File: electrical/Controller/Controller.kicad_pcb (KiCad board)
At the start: 2 copper layers, 72 x 20 mm, 30 parts, among them J1 USB4145-03-0170-C, J3 TC2030-NL, U1 LP5912-3.3DRV, U2 USBLC6-2P6, U3 STM32L072CBTx

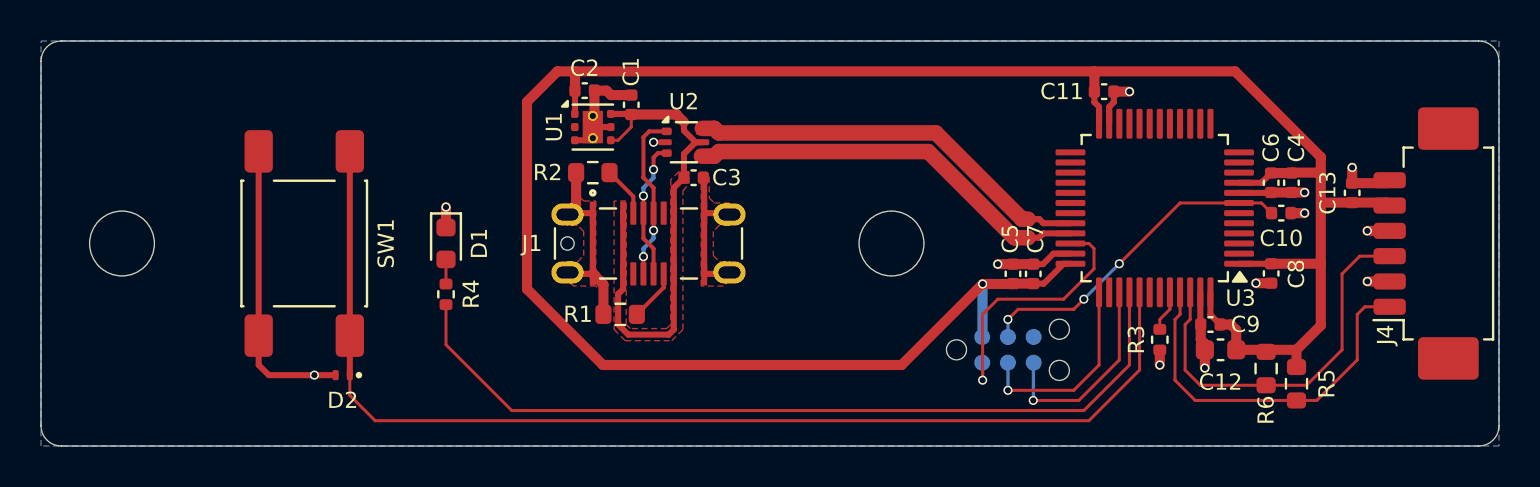
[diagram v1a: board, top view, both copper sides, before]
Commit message: Remove UART from debug connector
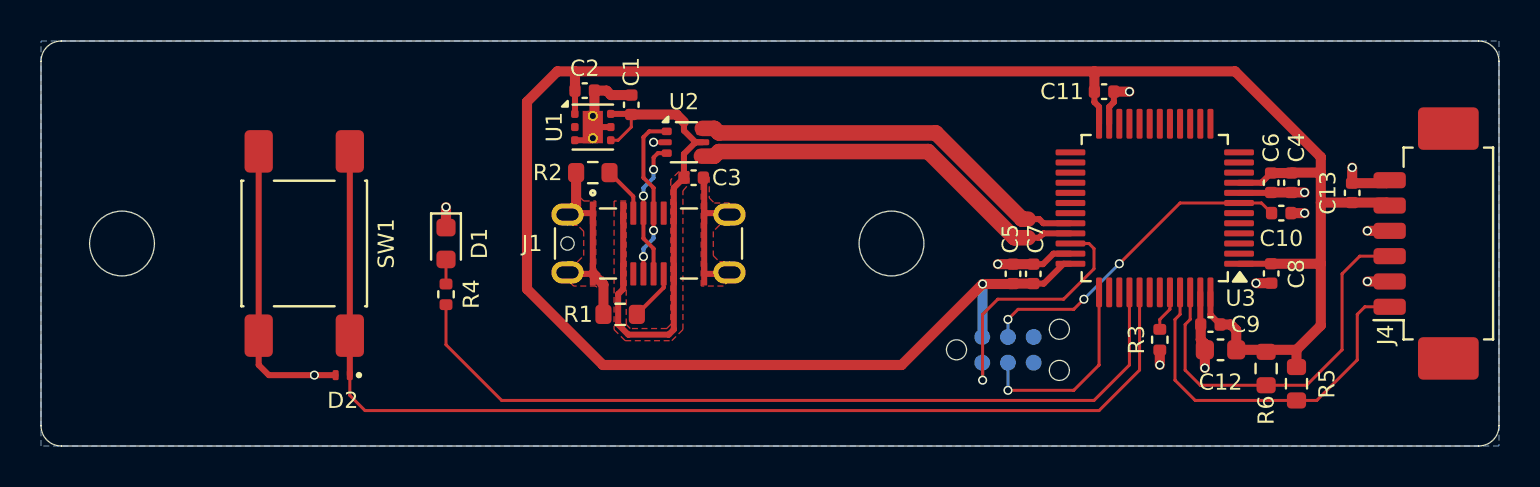
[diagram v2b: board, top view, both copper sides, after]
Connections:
- J3 pad 6: UART_TX -> unconnected-(J3-SWO-Pad6)
- U3 pad 39: UART_TX -> unconnected-(U3-PB3-Pad39)
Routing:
- net UART_TX: track 10.3 -> 0.00 mm, vias 1 -> 0
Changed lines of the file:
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@@
 	(net 10 "unconnected-(U3-PB14-Pad27)")
 	(net 11 "unconnected-(U3-PB13-Pad26)")
-	(net 12 "UART_TX")
+	(net 12 "unconnected-(J3-SWO-Pad6)")
 	(net 13 "/SWDIO")
 	(net 14 "/I2C_SCL")
@@
 	(net 51 "Net-(U3-PB4)")
 	(net 52 "Net-(D2-K)")
+	(net 53 "unconnected-(U3-PB3-Pad39)")
 	(footprint "MountingHole:MountingHole_3.2mm_M3"
 		(layer "F.Cu")
@@
 			(layers "F.Cu" "F.Mask" "F.Paste")
 			(roundrect_rratio 0.25)
-			(net 12 "UART_TX")
+			(net 53 "unconnected-(U3-PB3-Pad39)")
 			(pinfunction "PB3")
-			(pintype "bidirectional")
+			(pintype "bidirectional+no_connect")
 		)
 		(pad "40" smd roundrect
@@
 			(size 0.7874 0.7874)
 			(layers "B.Cu" "B.Mask")
-			(net 12 "UART_TX")
+			(net 12 "unconnected-(J3-SWO-Pad6)")
 			(pinfunction "SWO")
-			(pintype "input")
+			(pintype "input+no_connect")
 		)
 		(zone
@@
 	)
 	(segment
-		(start 167.25 86.75)
-		(end 169.25 84.75)
-		(width 0.15)
-		(layer "F.Cu")
-		(net 12)
-	)
-	(segment
-		(start 165 86.75)
-		(end 167.25 86.75)
-		(width 0.15)
-		(layer "F.Cu")
-		(net 12)
-	)
-	(segment
-		(start 169.25 84.75)
-		(end 169.25 81.4125)
-		(width 0.15)
-		(layer "F.Cu")
-		(net 12)
-	)
-	(via
-		(at 165 86.75)
-		(size 0.45)
-		(drill 0.3)
-		(layers "F.Cu" "B.Cu")
-		(net 12)
-	)
-	(segment
-		(start 165 84.905)
-		(end 165.02 84.885)
-		(width 0.15)
-		(layer "B.Cu")
-		(net 12)
-	)
-	(segment
-		(start 165 86.75)
-		(end 165 84.905)
-		(width 0.15)
-		(layer "B.Cu")
-		(net 12)
-	)
-	(segment
 		(start 168 80.25)
 		(end 168 79.25)
@@
 	)
 	(segment
-		(start 139.25 87.25)
-		(end 167.5 87.25)
+		(start 136 84)
+		(end 138.75 86.75)
 		(width 0.15)
 		(layer "F.Cu")
@@
 	)
 	(segment
-		(start 136 84)
-		(end 139.25 87.25)
+		(start 136 82.02)
+		(end 136 84)
 		(width 0.15)
 		(layer "F.Cu")
@@
 	)
 	(segment
-		(start 167.5 87.25)
+		(start 168 86.75)
 		(end 169.75 85)
 		(width 0.15)
@@
 	)
 	(segment
-		(start 169.75 85)
-		(end 169.75 81.4125)
+		(start 138.75 86.75)
+		(end 168 86.75)
 		(width 0.15)
 		(layer "F.Cu")
@@
 	)
 	(segment
-		(start 136 82.02)
-		(end 136 84)
+		(start 169.75 85)
+		(end 169.75 81.4125)
 		(width 0.15)
 		(layer "F.Cu")
@@
 	)
 	(segment
-		(start 131.25 86.5)
-		(end 131.25 85.5)
+		(start 170.25 81.4125)
+		(end 170.25 85.25)
 		(width 0.15)
 		(layer "F.Cu")
@@
 	)
 	(segment
-		(start 131.25 74.45)
-		(end 131.25 83.55)
-		(width 0.3)
+		(start 168.25 87.25)
+		(end 132 87.25)
+		(width 0.15)
 		(layer "F.Cu")
 		(net 52)
 	)
 	(segment
-		(start 170.25 81.4125)
-		(end 170.25 85.25)
+		(start 131.25 86.5)
+		(end 131.25 85.5)
 		(width 0.15)
 		(layer "F.Cu")
@@
 	)
 	(segment
-		(start 132.5 87.75)
-		(end 131.25 86.5)
+		(start 170.25 85.25)
+		(end 168.25 87.25)
 		(width 0.15)
 		(layer "F.Cu")
@@
 	)
 	(segment
-		(start 170.25 85.25)
-		(end 167.75 87.75)
-		(width 0.15)
+		(start 131.25 74.45)
+		(end 131.25 83.55)
+		(width 0.3)
 		(layer "F.Cu")
 		(net 52)
 	)
 	(segment
-		(start 167.75 87.75)
-		(end 132.5 87.75)
+		(start 132 87.25)
+		(end 131.25 86.5)
 		(width 0.15)
 		(layer "F.Cu")

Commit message: Use REVISION var to fill silkscreen
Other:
- board text added: "MIDI Concertina Controller - Rev ${REVISION}"
- board text removed: "MIDI Concertina Controller - Rev 1"
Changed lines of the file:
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@@
 		(layer "User.2")
 	)
-	(gr_text "MIDI Concertina Controller - Rev 1"
+	(gr_text "MIDI Concertina Controller - Rev ${REVISION}"
 		(at 187 70.25 0)
 		(layer "B.SilkS")

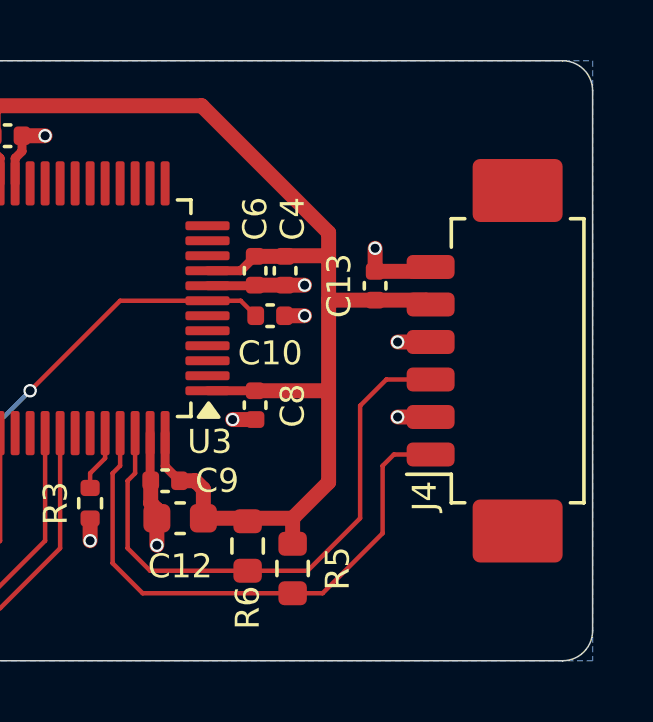
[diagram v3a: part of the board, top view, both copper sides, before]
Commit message: Replace PicoBlade connectors with SKEDD
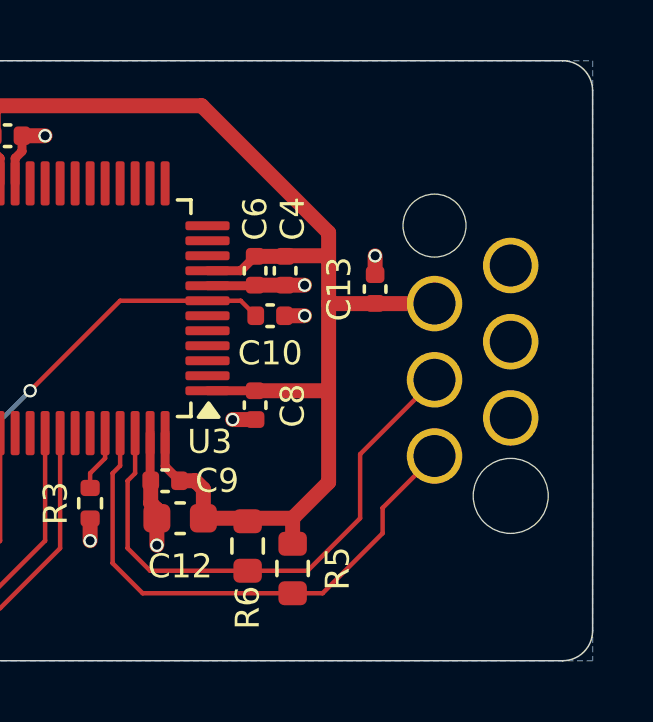
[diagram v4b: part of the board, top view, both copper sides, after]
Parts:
- J4: value ~ -> I2C; footprint Connector_Molex:Molex_PicoBlade_53261-0671_1x06-1MP_P1.25mm_Horizontal -> MidiConcertina:Wuerth_WR-WST_490107670612_2x03_P2.54mm_SKEDD; moved to B.Cu
- moved J4 1.00 mm to (184.0, 79.0), turned to 0 degrees
- moved C13 0.11 mm to (180.8, 76.6)
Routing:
- net GND: track 58.6 -> 54.4 mm, vias 13 -> 11
- net /I2C_SDA: track 19.2 -> 18.4 mm
- net /I2C_SCL: track 18.7 -> 18.0 mm
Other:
- board text added: "MIDI Concertina Controller Rev ${REVISION}"
- board text removed: "MIDI Concertina Controller - Rev ${REVISION}"

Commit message: Relabel components
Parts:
- renumbered J3 to J2, J4 to J3
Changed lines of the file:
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@@
 	(net 10 "unconnected-(U3-PB14-Pad27)")
 	(net 11 "unconnected-(U3-PB13-Pad26)")
-	(net 12 "unconnected-(J3-SWO-Pad6)")
+	(net 12 "unconnected-(J2-SWO-Pad6)")
 	(net 13 "/SWDIO")
 	(net 14 "/I2C_SCL")
@@
 		(layer "B.Cu")
 		(at 184 79)
-		(property "Reference" "J4"
+		(property "Reference" "J3"
 			(at -4 8 90)
 			(unlocked yes)
@@
 		(descr "Tag-Connect programming header; http://www.tag-connect.com/Materials/TC2030-IDC-NL.pdf")
 		(tags "tag connect programming header pogo pins")
-		(property "Reference" "J3"
+		(property "Reference" "J2"
 			(at -3.4 0 0)
 			(layer "B.SilkS")
@@
 			(size 0.7874 0.7874)
 			(layers "B.Cu" "B.Mask")
-			(net 12 "unconnected-(J3-SWO-Pad6)")
+			(net 12 "unconnected-(J2-SWO-Pad6)")
 			(pinfunction "SWO")
 			(pintype "input+no_connect")
